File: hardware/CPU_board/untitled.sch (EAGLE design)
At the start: 78 parts, among them IC1 MAX232ECWE, IC2 MAX232ECWE, IC3 AM29F040J, IC4 74HCT138D, IC5 LM2596S, IC6 74245SSOP, IC7 74245SSOP, IC8 74245SSOP, J2 POWER_JACKSLT, U1 AS6C4008-55SIN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

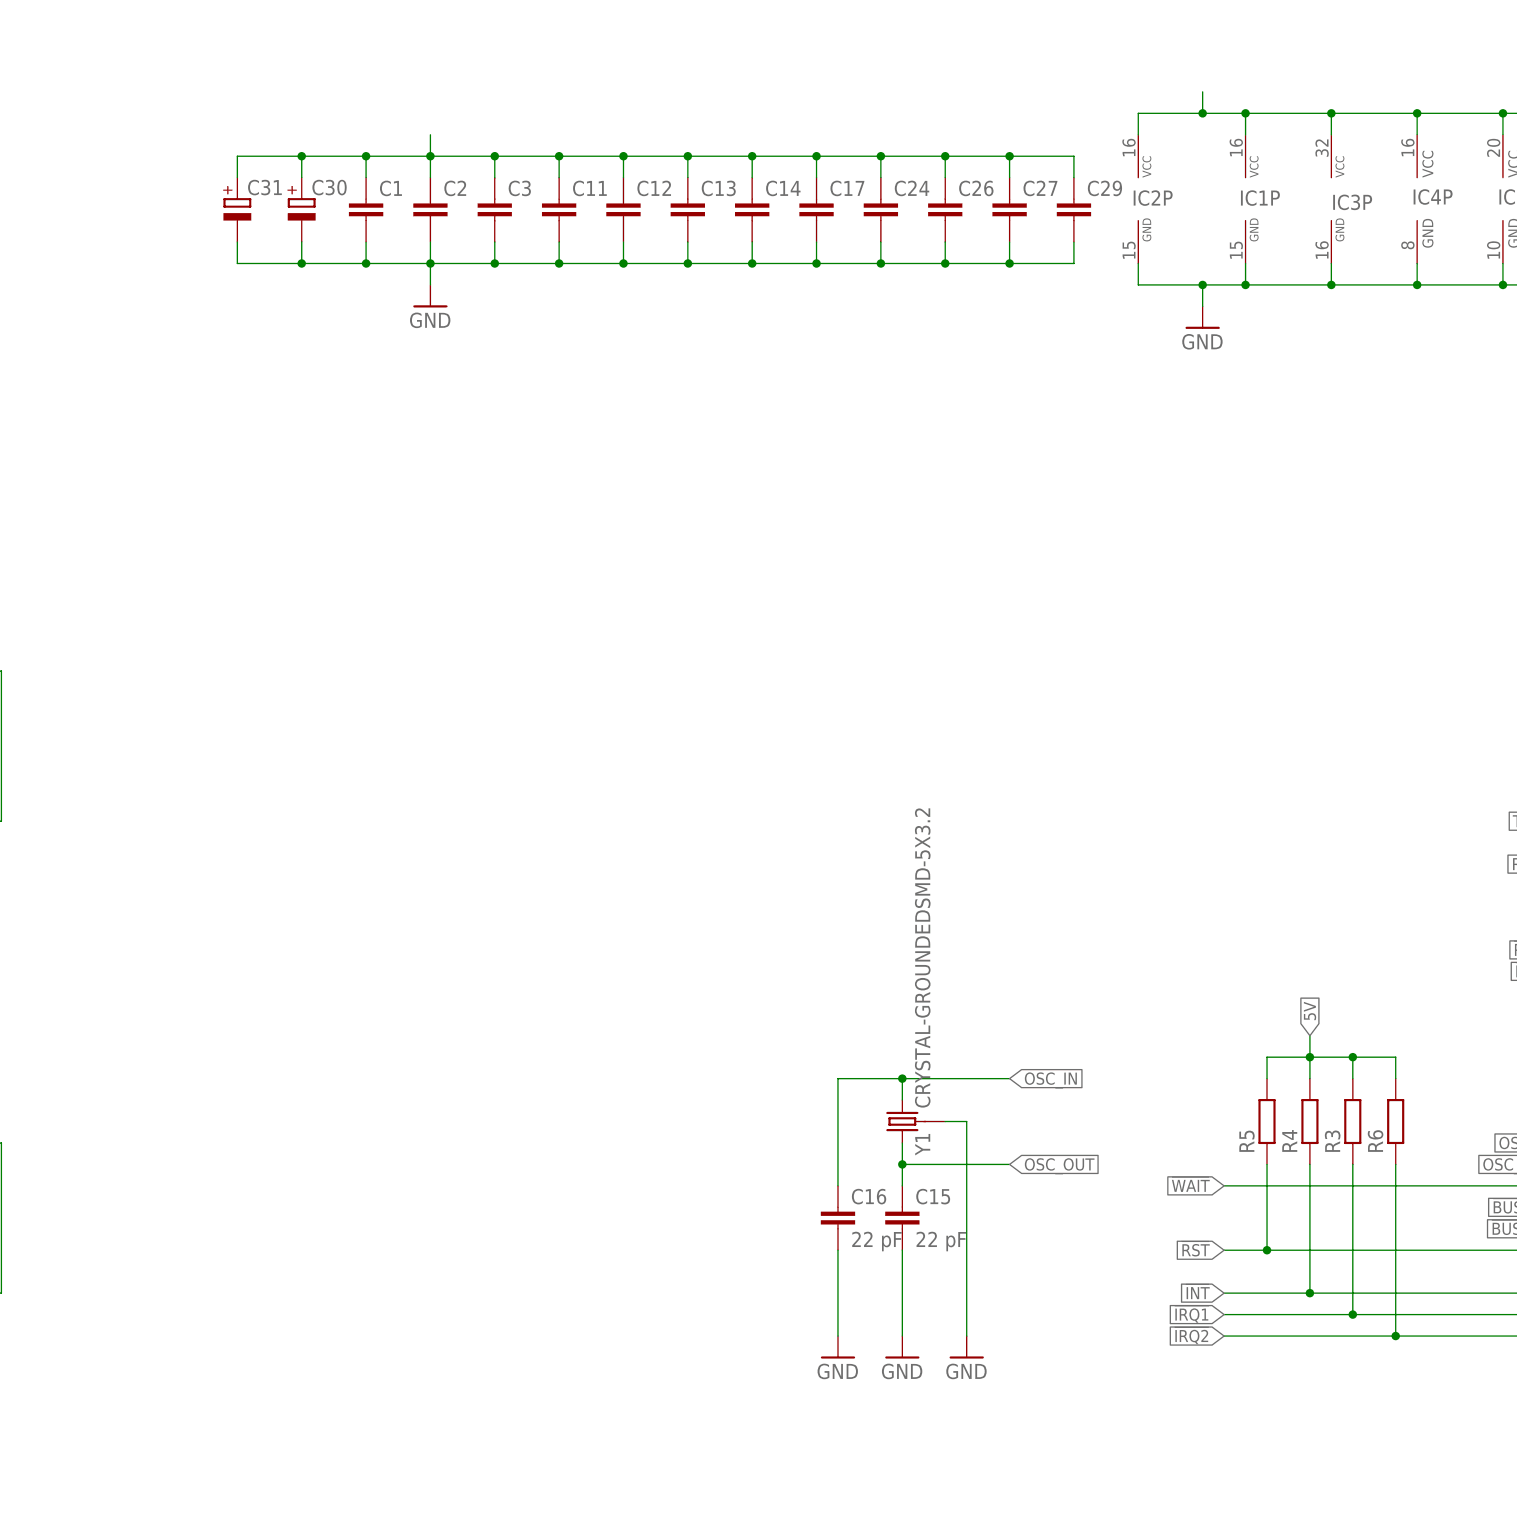
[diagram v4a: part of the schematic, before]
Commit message: Crystal resonator replaced with crystal generator
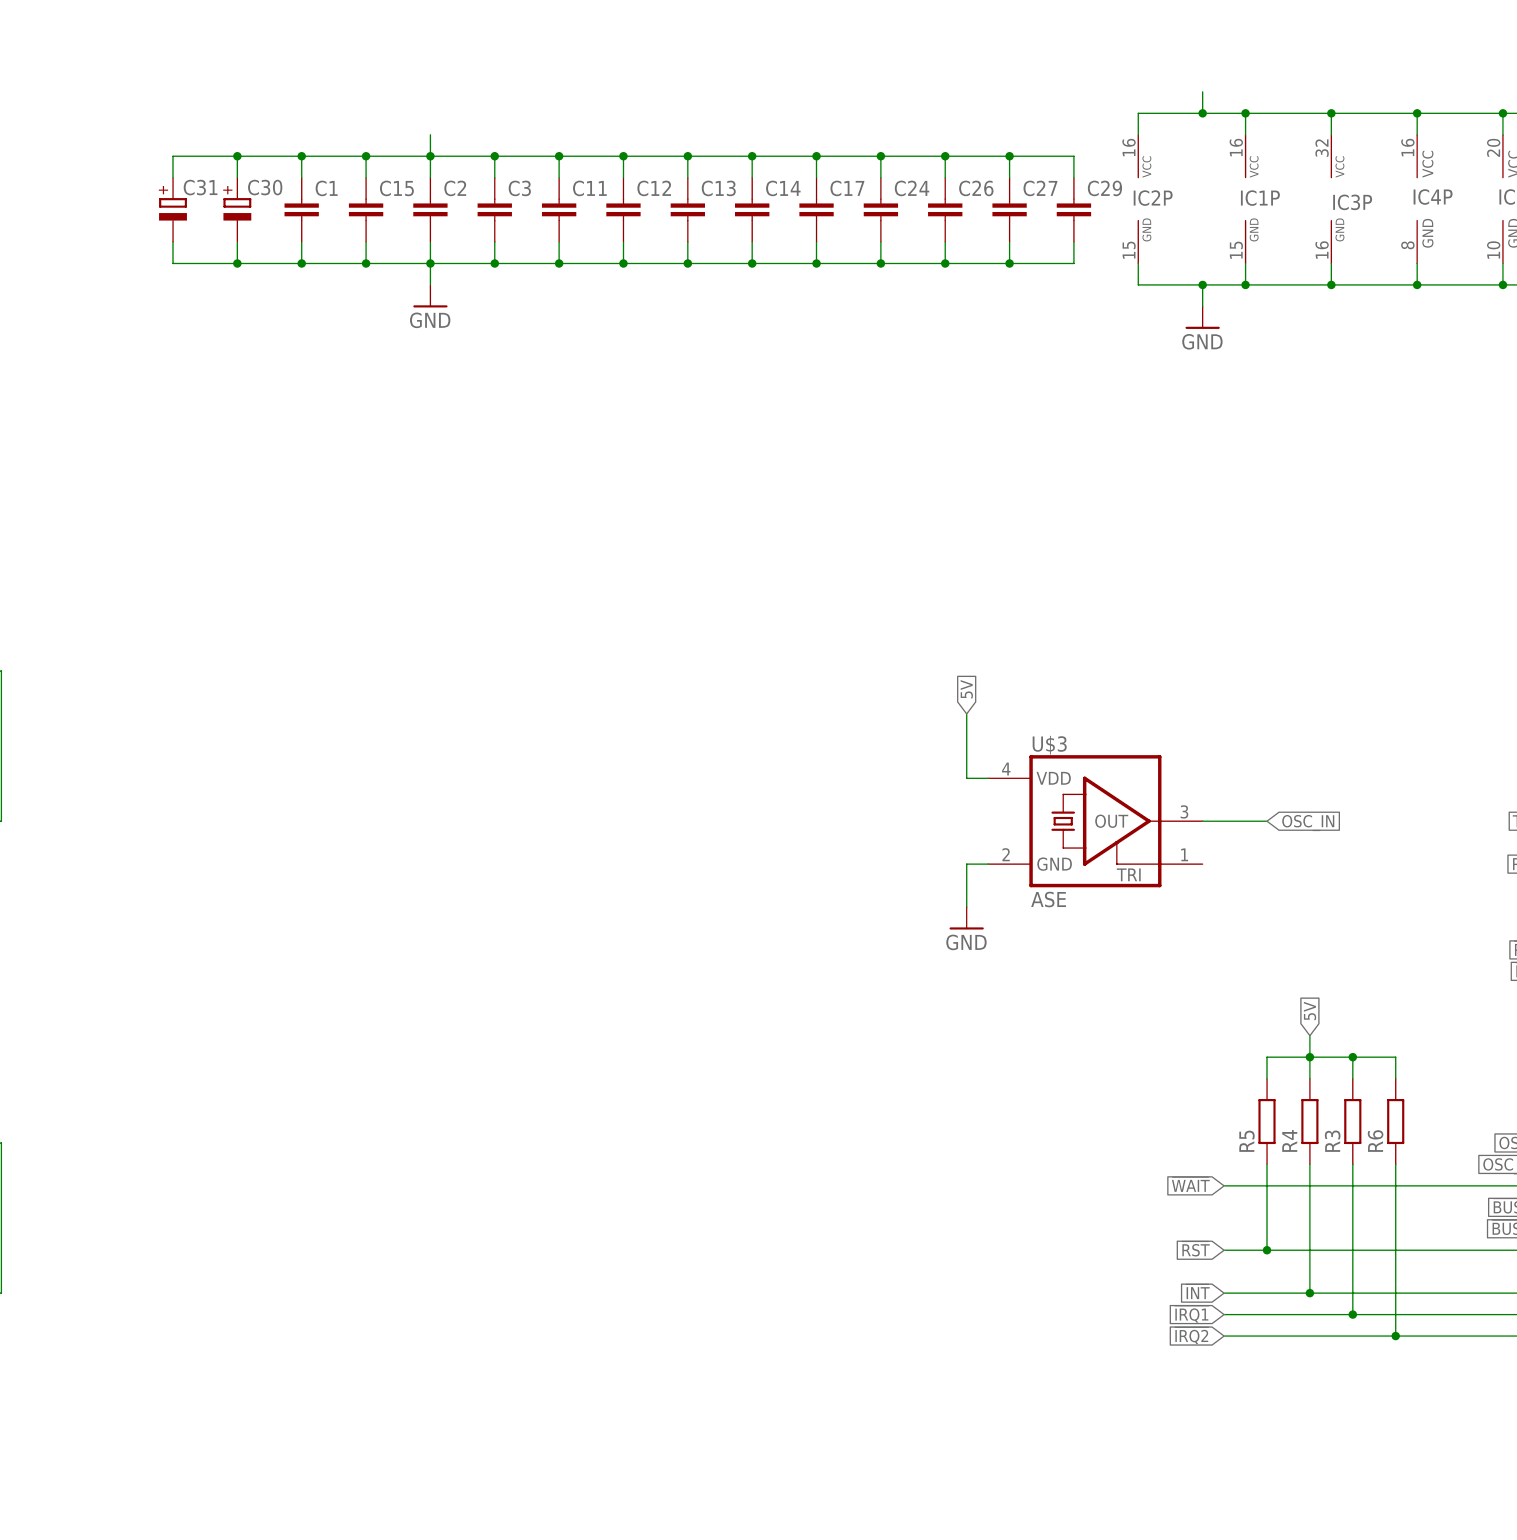
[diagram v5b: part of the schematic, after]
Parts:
- removed C16: 22 pF, rcl:C-EUC0603
- removed Y1: CRYSTAL-GROUNDEDSMD-5X3.2, SparkFun-Clocks:CRYSTAL-GROUNDEDSMD-5X3.2
- added U$3: ASE, crystal:ASE
- C15: value 22 pF -> (none)
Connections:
- net 5V: now also C15.1, U$3.VDD
- net GND: now also U$3.GND; no longer C16.2, Y1.3
- net OSC_IN: now also U$3.OUT; no longer C16.1, Y1.2
- net OSC_OUT: no longer C15.1, Y1.1
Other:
- moved on the sheet: C1, C15, C30, C31
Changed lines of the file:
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@@
 <part name="C13" library="rcl" deviceset="C-EU" device="C0402"/>
 <part name="C14" library="rcl" deviceset="C-EU" device="C0603"/>
-<part name="C15" library="rcl" deviceset="C-EU" device="C0603" value="22 pF"/>
-<part name="C16" library="rcl" deviceset="C-EU" device="C0603" value="22 pF"/>
-<part name="GND9" library="supply1" deviceset="GND" device=""/>
-<part name="GND35" library="supply1" deviceset="GND" device=""/>
-<part name="Y1" library="SparkFun-Clocks" deviceset="CRYSTAL-GROUNDED" device="SMD-5X3.2"/>
-<part name="GND17" library="supply1" deviceset="GND" device=""/>
 <part name="CON1" library="con-hirose" deviceset="CF-CARD-IDE_MODE" device=""/>
 <part name="GND19" library="supply1" deviceset="GND" device=""/>
@@
 <part name="JP10" library="pinhead" deviceset="PINHD-1X8" device=""/>
 <part name="JP11" library="pinhead" deviceset="PINHD-1X18" device=""/>
+<part name="U$3" library="crystal" deviceset="ASE" device=""/>
+<part name="GND74" library="supply1" deviceset="GND" device=""/>
+<part name="C15" library="rcl" deviceset="C-EU" device="C0603"/>
 </parts>
 <sheets>
@@
 <instance part="IC1" gate="P" x="-15.24" y="190.5"/>
 <instance part="GND4" gate="1" x="-20.32" y="175.26"/>
-<instance part="C1" gate="G$1" x="-119.38" y="190.5"/>
+<instance part="C1" gate="G$1" x="-127" y="190.5"/>
 <instance part="C2" gate="G$1" x="-111.76" y="190.5"/>
 <instance part="C3" gate="G$1" x="-104.14" y="190.5"/>
@@
 <instance part="C13" gate="G$1" x="-81.28" y="190.5"/>
 <instance part="C14" gate="G$1" x="-73.66" y="190.5"/>
-<instance part="C15" gate="G$1" x="-55.88" y="71.12"/>
-<instance part="C16" gate="G$1" x="-63.5" y="71.12"/>
-<instance part="GND9" gate="1" x="-55.88" y="53.34"/>
-<instance part="GND35" gate="1" x="-63.5" y="53.34"/>
-<instance part="Y1" gate="G$1" x="-55.88" y="81.28" rot="R90"/>
-<instance part="GND17" gate="1" x="-48.26" y="53.34"/>
 <instance part="CON1" gate="G$1" x="312.42" y="157.48"/>
 <instance part="GND19" gate="1" x="292.1" y="114.3"/>
@@
 <instance part="R15" gate="G$1" x="162.56" y="104.14"/>
 <instance part="C29" gate="G$1" x="-35.56" y="190.5"/>
-<instance part="C30" gate="G$1" x="-127" y="190.5"/>
-<instance part="C31" gate="G$1" x="-134.62" y="190.5"/>
+<instance part="C30" gate="G$1" x="-134.62" y="190.5"/>
+<instance part="C31" gate="G$1" x="-142.24" y="190.5"/>
 <instance part="LED4" gate="G$1" x="93.98" y="175.26"/>
 <instance part="R18" gate="G$1" x="93.98" y="162.56" rot="R90"/>
 <instance part="JP10" gate="A" x="464.82" y="177.8" rot="MR180"/>
 <instance part="JP11" gate="A" x="464.82" y="129.54" rot="MR180"/>
+<instance part="U$3" gate="G$1" x="-33.02" y="116.84"/>
+<instance part="GND74" gate="1" x="-48.26" y="104.14"/>
+<instance part="C15" gate="G$1" x="-119.38" y="190.5"/>
 </instances>
 <busses>
@@
 <segment>
 <pinref part="C1" gate="G$1" pin="2"/>
-<wire x1="-119.38" y1="185.42" x2="-119.38" y2="182.88" width="0.1524" layer="91"/>
+<wire x1="-127" y1="185.42" x2="-127" y2="182.88" width="0.1524" layer="91"/>
+<wire x1="-127" y1="182.88" x2="-119.38" y2="182.88" width="0.1524" layer="91"/>
+<pinref part="C3" gate="G$1" pin="2"/>
 <wire x1="-119.38" y1="182.88" x2="-111.76" y2="182.88" width="0.1524" layer="91"/>
-<pinref part="C3" gate="G$1" pin="2"/>
 <wire x1="-111.76" y1="182.88" x2="-104.14" y2="182.88" width="0.1524" layer="91"/>
 <wire x1="-104.14" y1="182.88" x2="-104.14" y2="185.42" width="0.1524" layer="91"/>
@@
 <junction x="-43.18" y="182.88"/>
 <pinref part="C30" gate="G$1" pin="-"/>
-<wire x1="-119.38" y1="182.88" x2="-127" y2="182.88" width="0.1524" layer="91"/>
-<wire x1="-127" y1="182.88" x2="-127" y2="185.42" width="0.1524" layer="91"/>
-<junction x="-119.38" y="182.88"/>
-<pinref part="C31" gate="G$1" pin="-"/>
 <wire x1="-127" y1="182.88" x2="-134.62" y2="182.88" width="0.1524" layer="91"/>
 <wire x1="-134.62" y1="182.88" x2="-134.62" y2="185.42" width="0.1524" layer="91"/>
 <junction x="-127" y="182.88"/>
+<pinref part="C31" gate="G$1" pin="-"/>
+<wire x1="-134.62" y1="182.88" x2="-142.24" y2="182.88" width="0.1524" layer="91"/>
+<wire x1="-142.24" y1="182.88" x2="-142.24" y2="185.42" width="0.1524" layer="91"/>
+<junction x="-134.62" y="182.88"/>
+<pinref part="C15" gate="G$1" pin="2"/>
+<wire x1="-119.38" y1="185.42" x2="-119.38" y2="182.88" width="0.1524" layer="91"/>
+<junction x="-119.38" y="182.88"/>
 </segment>
 <segment>
@@
 <wire x1="271.78" y1="-10.16" x2="269.24" y2="-10.16" width="0.1524" layer="91"/>
 <wire x1="269.24" y1="-10.16" x2="269.24" y2="-12.7" width="0.1524" layer="91"/>
-</segment>
-<segment>
-<pinref part="C15" gate="G$1" pin="2"/>
-<pinref part="GND9" gate="1" pin="GND"/>
-<wire x1="-55.88" y1="55.88" x2="-55.88" y2="66.04" width="0.1524" layer="91"/>
-</segment>
-<segment>
-<pinref part="C16" gate="G$1" pin="2"/>
-<pinref part="GND35" gate="1" pin="GND"/>
-<wire x1="-63.5" y1="55.88" x2="-63.5" y2="66.04" width="0.1524" layer="91"/>
-</segment>
-<segment>
-<pinref part="Y1" gate="G$1" pin="3"/>
-<pinref part="GND17" gate="1" pin="GND"/>
-<wire x1="-50.8" y1="81.28" x2="-48.26" y2="81.28" width="0.1524" layer="91"/>
-<wire x1="-48.26" y1="81.28" x2="-48.26" y2="55.88" width="0.1524" layer="91"/>
 </segment>
 <segment>
@@
 <pinref part="GND26" gate="1" pin="GND"/>
 </segment>
+<segment>
+<pinref part="U$3" gate="G$1" pin="GND"/>
+<pinref part="GND74" gate="1" pin="GND"/>
+<wire x1="-45.72" y1="111.76" x2="-48.26" y2="111.76" width="0.1524" layer="91"/>
+<wire x1="-48.26" y1="111.76" x2="-48.26" y2="106.68" width="0.1524" layer="91"/>
+</segment>
 </net>
 <net name="5V" class="0">
@@
 <segment>
 <pinref part="C1" gate="G$1" pin="1"/>
-<wire x1="-119.38" y1="193.04" x2="-119.38" y2="195.58" width="0.1524" layer="91"/>
+<wire x1="-127" y1="193.04" x2="-127" y2="195.58" width="0.1524" layer="91"/>
+<wire x1="-127" y1="195.58" x2="-119.38" y2="195.58" width="0.1524" layer="91"/>
+<pinref part="C3" gate="G$1" pin="1"/>
 <wire x1="-119.38" y1="195.58" x2="-111.76" y2="195.58" width="0.1524" layer="91"/>
-<pinref part="C3" gate="G$1" pin="1"/>
 <wire x1="-111.76" y1="195.58" x2="-104.14" y2="195.58" width="0.1524" layer="91"/>
 <wire x1="-104.14" y1="195.58" x2="-104.14" y2="193.04" width="0.1524" layer="91"/>
@@
 <junction x="-43.18" y="195.58"/>
 <pinref part="C30" gate="G$1" pin="+"/>
-<wire x1="-119.38" y1="195.58" x2="-127" y2="195.58" width="0.1524" layer="91"/>
-<wire x1="-127" y1="195.58" x2="-127" y2="193.04" width="0.1524" layer="91"/>
-<junction x="-119.38" y="195.58"/>
-<pinref part="C31" gate="G$1" pin="+"/>
 <wire x1="-127" y1="195.58" x2="-134.62" y2="195.58" width="0.1524" layer="91"/>
 <wire x1="-134.62" y1="195.58" x2="-134.62" y2="193.04" width="0.1524" layer="91"/>
 <junction x="-127" y="195.58"/>
+<pinref part="C31" gate="G$1" pin="+"/>
+<wire x1="-134.62" y1="195.58" x2="-142.24" y2="195.58" width="0.1524" layer="91"/>
+<wire x1="-142.24" y1="195.58" x2="-142.24" y2="193.04" width="0.1524" layer="91"/>
+<junction x="-134.62" y="195.58"/>
+<pinref part="C15" gate="G$1" pin="1"/>
+<wire x1="-119.38" y1="193.04" x2="-119.38" y2="195.58" width="0.1524" layer="91"/>
+<junction x="-119.38" y="195.58"/>
 </segment>
 <segment>
@@
 <label x="93.98" y="182.88" size="1.4224" layer="95" rot="R90" xref="yes"/>
 </segment>
+<segment>
+<pinref part="U$3" gate="G$1" pin="VDD"/>
+<wire x1="-45.72" y1="121.92" x2="-48.26" y2="121.92" width="0.1524" layer="91"/>
+<wire x1="-48.26" y1="121.92" x2="-48.26" y2="129.54" width="0.1524" layer="91"/>
+<label x="-48.26" y="129.54" size="1.4224" layer="95" rot="R90" xref="yes"/>
+</segment>
 </net>
 <net name="TXD1" class="0">
@@
 <net name="OSC_OUT" class="0">
 <segment>
-<wire x1="-55.88" y1="76.2" x2="-55.88" y2="78.74" width="0.1524" layer="91"/>
-<pinref part="C15" gate="G$1" pin="1"/>
-<wire x1="-55.88" y1="76.2" x2="-55.88" y2="73.66" width="0.1524" layer="91"/>
-<junction x="-55.88" y="76.2"/>
-<pinref part="Y1" gate="G$1" pin="1"/>
-<wire x1="-43.18" y1="76.2" x2="-55.88" y2="76.2" width="0.1524" layer="91"/>
-<label x="-43.18" y="76.2" size="1.4224" layer="95" xref="yes"/>
-</segment>
-<segment>
 <pinref part="U$1" gate="G$1" pin="EXTAL"/>
 <wire x1="35.56" y1="76.2" x2="22.86" y2="76.2" width="0.1524" layer="91"/>
@@
 <net name="OSC_IN" class="0">
 <segment>
-<wire x1="-55.88" y1="86.36" x2="-55.88" y2="83.82" width="0.1524" layer="91"/>
-<pinref part="C16" gate="G$1" pin="1"/>
-<wire x1="-55.88" y1="86.36" x2="-63.5" y2="86.36" width="0.1524" layer="91"/>
-<wire x1="-63.5" y1="86.36" x2="-63.5" y2="73.66" width="0.1524" layer="91"/>
-<junction x="-55.88" y="86.36"/>
-<pinref part="Y1" gate="G$1" pin="2"/>
-<wire x1="-43.18" y1="86.36" x2="-55.88" y2="86.36" width="0.1524" layer="91"/>
-<label x="-43.18" y="86.36" size="1.4224" layer="95" xref="yes"/>
-</segment>
-<segment>
 <pinref part="U$1" gate="G$1" pin="XTAL"/>
 <wire x1="35.56" y1="78.74" x2="22.86" y2="78.74" width="0.1524" layer="91"/>
 <label x="22.86" y="78.74" size="1.4224" layer="95" rot="R180" xref="yes"/>
 </segment>
-</net>
+<segment>
+<pinref part="U$3" gate="G$1" pin="OUT"/>
+<wire x1="-20.32" y1="116.84" x2="-12.7" y2="116.84" width="0.1524" layer="91"/>
+<label x="-12.7" y="116.84" size="1.4224" layer="95" rot="MR180" xref="yes"/>
+</segment>
+</net>

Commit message: PCB updated
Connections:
- removed net CF6: JP2.8
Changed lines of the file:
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@@
 <wire x1="-96.52" y1="266.7" x2="-96.52" y2="274.32" width="0.1524" layer="91"/>
 <junction x="-96.52" y="274.32"/>
+<label x="-88.9" y="274.32" size="1.4224" layer="95" xref="yes"/>
 </segment>
 <segment>
@@
 <pinref part="RN1" gate="A" pin="1"/>
 <wire x1="444.5" y1="40.64" x2="444.5" y2="45.72" width="0.1524" layer="91"/>
+<label x="444.5" y="45.72" size="1.4224" layer="95" rot="R90" xref="yes"/>
 </segment>
 <segment>
@@
 <wire x1="-66.04" y1="266.7" x2="-73.66" y2="266.7" width="0.1524" layer="91"/>
 <wire x1="-73.66" y1="266.7" x2="-73.66" y2="274.32" width="0.1524" layer="91"/>
+<label x="-73.66" y="274.32" size="1.4224" layer="95" rot="R90" xref="yes"/>
 </segment>
 <segment>
@@
 <pinref part="R14" gate="G$1" pin="2"/>
 <wire x1="55.88" y1="20.32" x2="55.88" y2="17.78" width="0.1524" layer="91"/>
+<label x="55.88" y="17.78" size="1.4224" layer="95" rot="R270" xref="yes"/>
 </segment>
 <segment>
@@
 </segment>
 </net>
-<net name="CF6" class="0">
-<segment>
-<pinref part="JP2" gate="A" pin="8"/>
-<wire x1="464.82" y1="60.96" x2="472.44" y2="60.96" width="0.1524" layer="91"/>
-<label x="472.44" y="60.96" size="1.4224" layer="95" xref="yes"/>
-</segment>
-</net>
